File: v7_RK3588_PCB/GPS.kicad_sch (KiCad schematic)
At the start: 0 parts

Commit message: add GPS schematic
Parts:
- added C6001: 33nF/6.3V, symbol Device:C
- added C6002: 100nF/6.3V, symbol Device:C
- added C6003: 10uF/6.3V, symbol Device:C
- added C6004, C6005: C, symbol Device:C
- added CR?: SP1005-01ETG, CR_SOD882_LTF, symbol SP1005_01ETG:SP1005-01ETG
- added D6001: RCLAMP0501T, symbol Device:D_TVS
- added E?: APAE1575R1820ABDC1-T, APAE1575R1820ABDC1-T:XDCR_APAE1575R1820ABDC1-T, symbol APAE1575R1820ABDC1-T:APAE1575R1820ABDC1-T
- added R6001, R6002: 0, symbol Device:R
- added U6001: LC76GABMD, LC76G_QWS, symbol LC76GABMD:LC76GABMD
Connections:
- new net: C6004.1, R6002.1, U6001.11 (RF_IN)
- new net: C6005.1, CR?.2, E?.1, R6002.2
- new net: R6001.2, U6001.9 (RESET_N)
- new net GND: C6001.2, C6002.2, C6003.2, C6004.2, C6005.2, CR?.1, D6001.1 (A1), U6001.1 (GND), U6001.10 (GND), U6001.12 (GND), U6001.28 (GND)
- new net GPS_1PPS: U6001.4 (1PPS)
- new net GPS_3D_FIX_GPIO: U6001.23 (*3D_FIX)
- new net GPS_JAM_IND_GPIO: U6001.22 (JAM_IND)
- new net GPS_RESET_GPIO: R6001.1
- new net I2C2_SCL_GPS: U6001.17 (I2C_SCL)
- new net I2C2_SDA_GPS: U6001.16 (I2C_SDA)
- new net VCC_3V3: C6001.1, C6002.1, C6003.1, D6001.2 (A2), U6001.6 (V_BCKP), U6001.8 (VCC)
- no-connect marks 0 -> 11
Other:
- note added: "Checked: Ema"
- note added: "HIGH Logic Level is 1.8V through 3.6V"
- note added: "Matching required"
- note added: "TODO: Pullup resistors on RK3588 page"

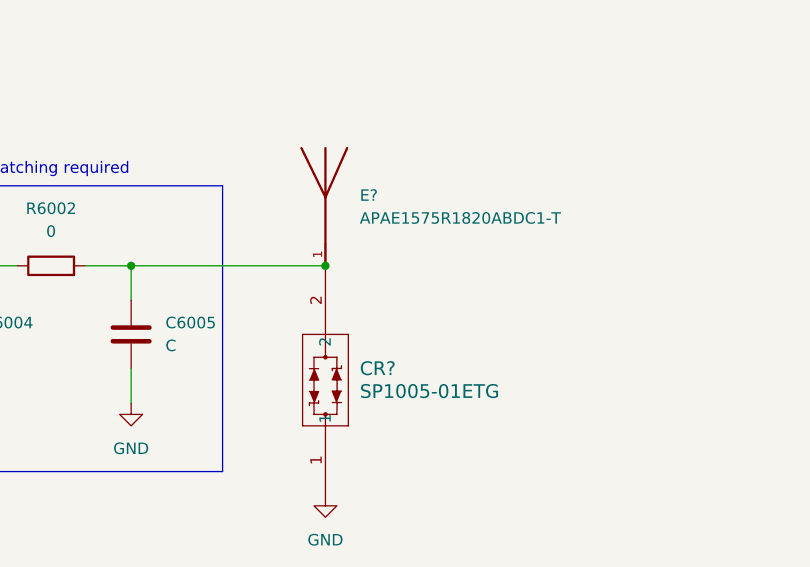
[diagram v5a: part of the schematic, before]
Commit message: add power sequencing
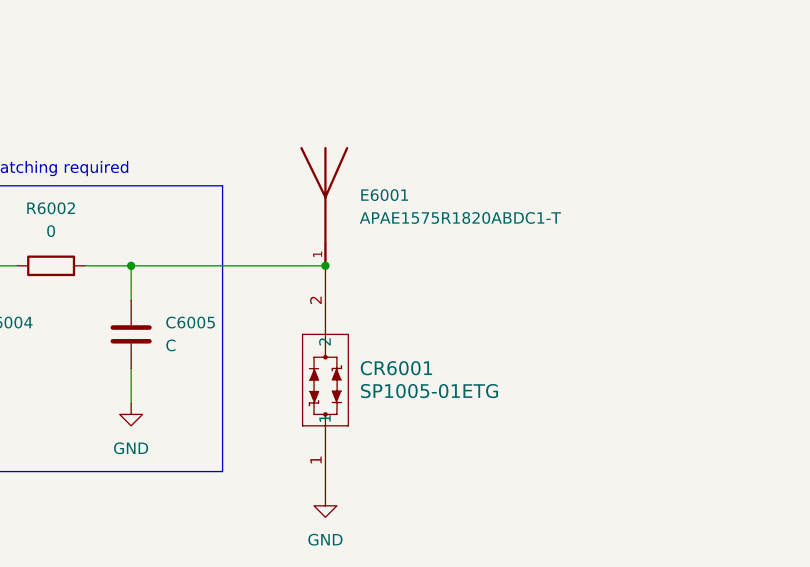
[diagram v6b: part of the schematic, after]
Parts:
- CR6001: renamed from CR?; footprint CR_SOD882_LTF -> (none)
- U6001: footprint LC76G_QWS -> (none)
- gave numbers to parts that had none: 1
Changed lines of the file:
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@@
 		(dnp no)
 		(fields_autoplaced yes)
-		(property "Reference" "E?"
+		(property "Reference" "E6001"
 			(at 130.81 144.5894 0)
 			(effects
@@
 			(project "v7_RK3588_PCB"
 				(path "/1d5a1342-f497-4807-8bdb-ea718133b0ad/47f846f7-67f6-44ee-b9eb-cd197539bf38"
-					(reference "E?")
+					(reference "E6001")
 					(unit 1)
 				)
@@
 			)
 		)
-		(property "Footprint" "LC76G_QWS"
+		(property "Footprint" ""
 			(at 81.28 78.74 0)
 			(effects
@@
 		(dnp no)
 		(fields_autoplaced yes)
-		(property "Reference" "CR?"
+		(property "Reference" "CR6001"
 			(at 130.81 163.8299 90)
 			(effects
@@
 			)
 		)
-		(property "Footprint" "CR_SOD882_LTF"
+		(property "Footprint" ""
 			(at 127 177.8 0)
 			(effects
@@
 			(project "v7_RK3588_PCB"
 				(path "/1d5a1342-f497-4807-8bdb-ea718133b0ad/47f846f7-67f6-44ee-b9eb-cd197539bf38"
-					(reference "CR?")
-					(unit 1)
-				)
+					(reference "CR6001")
+					(unit 1)
+				)
